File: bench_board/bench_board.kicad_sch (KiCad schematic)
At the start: 55 parts, among them J1 BATT_4S, J2 BOOT0_JUMPER, J3 USB-C, J4 CRSF_UART, J5 DSHOT_M1-M4, J6 SWD, J7 RX_PWR_5V, J8 TELEM_TX, J9 EXPANSION_BUS, U1 STM32F405RGT6, U2 TPS54336ADDA, U4 MPU-6000, U5 USBLC6-2SC6, U6 MT3608, Y1 8MHz

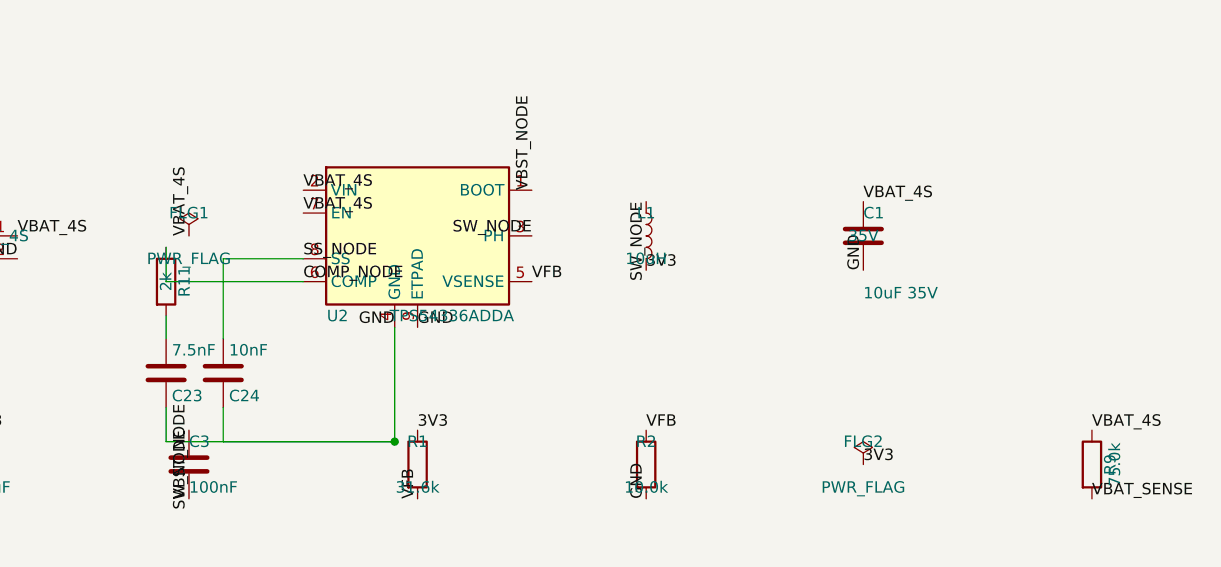
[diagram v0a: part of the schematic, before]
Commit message: Item 2: board blocker burn-down -- C23, Y1, C1, holes, net parity
BLOCKER 4 CLEARED -- C23's net existed nowhere. The buck's compensation
network is COMP_NODE -> R11 -> [nothing] -> C23 -> GND: the junction
between R11 pin 2 and C23 pin 1 had no wire, so the TPS54336's control
loop was not connected. Added the wire and a COMP_RC net label; ERC still
0/0, and the net now appears on the board (52 nets, was 51). C23 is gone
from the parity report.

Y1 -- the board carried a 4-pin 3225 crystal footprint under a 2-PIN
schematic symbol, which is why pads 3/4 were permanently unmatched in
every sync. The only Basic-library 8MHz part (C115962) is a 2-pin
SMD-5032. Delete-and-replaced to Crystal_SMD_5032-2Pin_5.0x3.2mm: fixes
the pad mismatch AND removes a JLCPCB Extended setup fee. Pad count
verified 2.

C1 -- respecified per the review's correction. The old note confused
voltage rating with DC-bias derating. Now 1210 / 50V / X7R (Murata
GRM32ER71H106KA12L) with the requirement written as CAPACITANCE AT
16.8V BIAS and an explicit instruction to read the vendor's C-vs-Vdc
curve before ordering. Footprint delete-and-replaced 0805 -> 1210.

MOUNTING HOLES -- fixing a defect I introduced last batch. The 30.5x30.5
pattern placed them ON TOP of nine components (D1, J2, R12, R13, C2, J4,
L1, R1, U2, C6, J6, R3): I validated one component's position virtually
and never re-ran the full overlap check after placing the holes. Moved
to (4.5,19), (75.5,16), (4.5,55.5), (75.5,41) -- found by scanning every
courtyard, verified 0 overlaps. Also moved Y1 and L1, which were
overlapping U1 and U2. Board is now 0 courtyard overlaps. MH silkscreen
text hidden (its bbox is 20mm wide for a 6mm hole and hung off the edge).

NET PARITY -- 262 -> 88 parity issues. All 199 net_conflicts were the
same uniform difference: the board stored bare net names, KiCad's
netlister uses the sheet-path form (GND vs /GND), across 52 nets with no
genuine mismatch hiding among them. Renamed every board net reference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
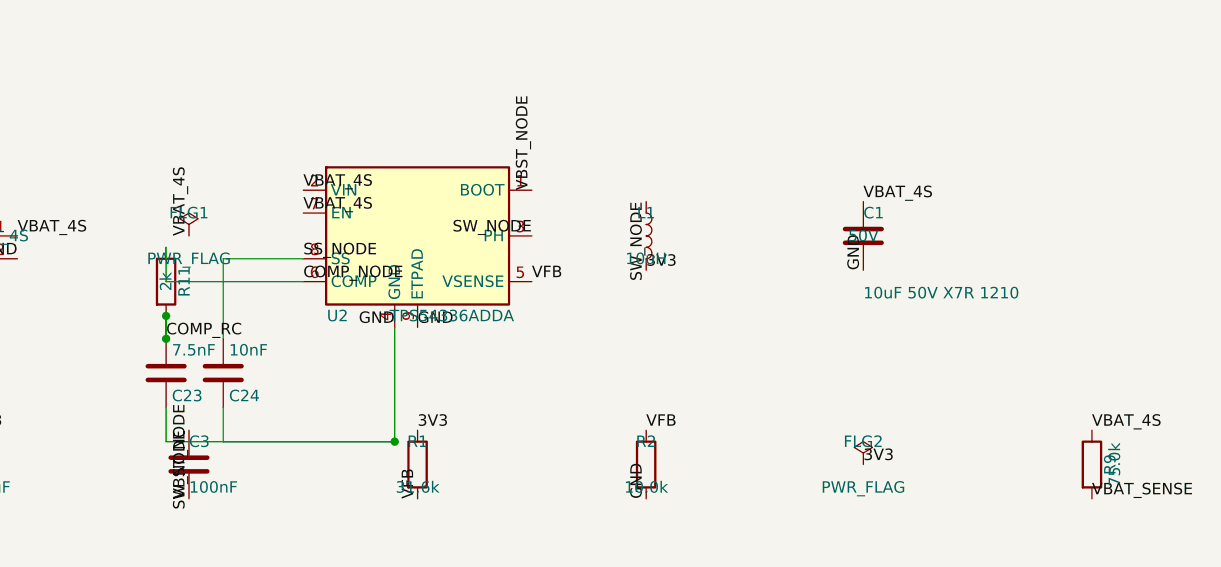
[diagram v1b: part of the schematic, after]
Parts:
- C1: value 10uF 35V -> 10uF 50V X7R 1210; footprint Capacitor_SMD:C_0805_2012Metric -> Capacitor_SMD:C_1210_3225Metric; Dielectric (none) -> X7R; MPN (none) -> GRM32ER71H106KA12L; Manufacturer (none) -> Murata; Notes (none) -> VBAT_4S input bulk, 16.8V max. SPEC IS CAPACITANCE AT BIAS,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; Voltage 35V -> 50V
- Y1: footprint Crystal:Crystal_SMD_3225-4Pin_3.2x2.5mm -> Crystal:Crystal_SMD_5032-2Pin_5.0x3.2mm; JLCPCB_PN (none) -> C115962; LCSC (none) -> C115962; Manufacturer (none) -> TXC; Notes (none) -> 8MHz +/-10ppm, SMD-5032-2P. Switched from a 3225-4Pin footp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
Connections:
- net COMP_RC: now reaches C23.1, R11.2
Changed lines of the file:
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@@
 			)
 		)
-		(property "Value" "10uF 35V"
+		(property "Value" "10uF 50V X7R 1210"
 			(at 449.58 55.88 0)
 			(show_name no)
@@
 			)
 		)
-		(property "Footprint" "Capacitor_SMD:C_0805_2012Metric"
+		(property "Footprint" "Capacitor_SMD:C_1210_3225Metric"
 			(at 450.545 45.72 0)
 			(hide yes)
@@
 			)
 		)
-		(property "Voltage" "35V"
+		(property "Voltage" "50V"
 			(at 449.58 49.53 0)
 			(effects
@@
 			)
 		)
+    (property "Dielectric" "X7R" (at 449.58 49.53 0)
+      (effects (font (size 1.27 1.27)) (hide yes))
+    )
+    (property "Manufacturer" "Murata" (at 449.58 49.53 0)
+      (effects (font (size 1.27 1.27)) (hide yes))
+    )
+    (property "MPN" "GRM32ER71H106KA12L" (at 449.58 49.53 0)
+      (effects (font (size 1.27 1.27)) (hide yes))
+    )
+    (property "Notes" "VBAT_4S input bulk, 16.8V max. SPEC IS CAPACITANCE AT BIAS, NOT NAMEPLATE: an MLCC's value collapses under DC bias regardless of its voltage rating, so '10uF' alone is meaningless here. Was 0805 25V, which at 16.8V retains only a small fraction. Moved to 1210/50V X7R on 2026-08-17 because bias derating is driven by case size and dielectric, not by the rating. MUST VERIFY the derated value on Murata SimSurfing (or the vendor's own C-vs-Vdc curve) before ordering and confirm it meets the TPS54336A input-capacitance requirement; do not accept a substitute chosen on nameplate value alone." (at 449.58 49.53 0)
+      (effects (font (size 1.27 1.27)) (hide yes))
+    )
 		(pin "1"
 		)
@@
 			)
 		)
-		(property "Footprint" "Crystal:Crystal_SMD_3225-4Pin_3.2x2.5mm"
+		(property "Footprint" "Crystal:Crystal_SMD_5032-2Pin_5.0x3.2mm"
 			(at 449.58 199.39 0)
 			(hide yes)
@@
 			)
 		)
+    (property "LCSC" "C115962" (at 449.58 199.39 0)
+      (effects (font (size 1.27 1.27)) (hide yes))
+    )
+    (property "JLCPCB_PN" "C115962" (at 449.58 199.39 0)
+      (effects (font (size 1.27 1.27)) (hide yes))
+    )
+    (property "Manufacturer" "TXC" (at 449.58 199.39 0)
+      (effects (font (size 1.27 1.27)) (hide yes))
+    )
+    (property "Notes" "8MHz +/-10ppm, SMD-5032-2P. Switched from a 3225-4Pin footprint 2026-08-17: the symbol is a 2-pin crystal, so the 4-pin footprint left pads 3/4 permanently unmatched, and the only Basic-library 8MHz part is this 2-pin 5032. Verify the part number against a live JLCPCB page before ordering -- it came from a community snapshot of the Basic library, not an authoritative source." (at 449.58 199.39 0)
+      (effects (font (size 1.27 1.27)) (hide yes))
+    )
 		(pin "1"
 		)
@@
 		(effects
 			(font
+				(size 1.27 1.27)
+			)
+			(justify left bottom)
+		)
+	)
+	(wire
+		(pts
+			(xy 372.11 58.42) (xy 372.11 60.959999999999994)
+		)
+		(stroke
+			(width 0)
+			(type default)
+		)
+	)
+	(junction
+		(at 372.11 58.42)
+		(diameter 0)
+		(color 0 0 0 0)
+	)
+	(junction
+		(at 372.11 60.96)
+		(diameter 0)
+		(color 0 0 0 0)
+	)
+	(label "COMP_RC"
+		(at 372.11 60.959999999999994 0)
+		(effects
+			(font

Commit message: Item 5 (hardware): buzzer on PA8 -- low-side MOSFET, placed and part-routed
Q1 AO3400A low-side switch, R14 100R gate series, R15 10k pull-down, D2
1N4148W flyback, C27 10uF local bulk, J10 2-pin header. PA8 chosen over
several other free GPIOs because it is TIM1_CH1 and TIM1 is unused, so a
passive buzzer with real tones stays possible with no board change. PA8's
stale no-connect flag removed; ERC is 0/0.

An F4 pin is rated 25 mA and a 12 mm buzzer draws 30-90 mA, so the FET is
not optional. D2 is fitted even though a piezo buzzer would not need it --
two cents to make the board buzzer-type-independent.

THE PLACEMENT WAS WRONG FIRST TIME. Q1 and C27 landed on top of a 15.7 mm
NRST track from J6 pin 4; DRC caught it as a /NRST <-> /BUZZER_SW short.
The region had been picked by reading the component list, and a component
list says nothing about routed copper -- check_placement_clearance does
not either, it classifies bodies and courtyards, not tracks.

scripts/padclear.py now measures every new pad against every segment and
via on the layers that pad occupies. It then caught two more that would
have shipped: a /BUZZER_SW diagonal passing 0.011 mm from J10's 5V pad,
and a GND via sited OUTSIDE the GND pour (the pour stops at y~58.0) --
the same class as this project's earlier fanout-via blocker, fixed the
same way, point-in-polygon against real filled_polygon geometry. The
checker itself had the KiCad rotation sign backwards on first use and was
verifying J10's pads at mirrored coordinates; corrected.

Routed and verified: BUZZER_GATE, BUZZER_SW, the local 5V chain, and GND
with two stitching vias both confirmed >=0.60 mm inside the GND pour.
NOT routed: BUZZER_GPIO (U1.41 -> R14.1, ~20 mm across the busy area) and
the 5V feed from J7. Until the first of those exists the buzzer cannot be
driven at all, which the doc says in those words.

kicad-cli DRC 46 -> 64, unconnected 13 -> 15. The +2 unconnected are
exactly the two nets above. +12 of the +18 violations are th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
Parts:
- added C27: 10uF 16V, Capacitor_SMD:C_0805_2012Metric, symbol Device:C
- added D2: 1N4148W, Diode_SMD:D_SOD-123, symbol Diode:1N4148W
- added J10: BUZZER, Connector_PinHeader_2.54mm:PinHeader_1x02_P2.54mm_Vertical, symbol Connector:Conn_01x02_Pin
- added Q1: AO3400A, Package_TO_SOT_SMD:SOT-23, symbol Transistor_FET:AO3400A
- added R14: 100R, Resistor_SMD:R_0402_1005Metric, symbol Device:R
- added R15: 10k, Resistor_SMD:R_0402_1005Metric, symbol Device:R
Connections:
- net 5V_RX: now also C27.1, D2.1 (K), J10.1 (Pin_1)
- net GND: now also C27.2, Q1.2 (S), R15.2
- net BUZZER_GPIO: now reaches U1.41 (PA8)
- net BUZZER_GPIO: now also R14.1
- new net BUZZER_GATE: Q1.1 (G), R14.2, R15.1
- new net BUZZER_SW: D2.2 (A), J10.2 (Pin_2), Q1.3 (D)
- no-connect marks 24 -> 23

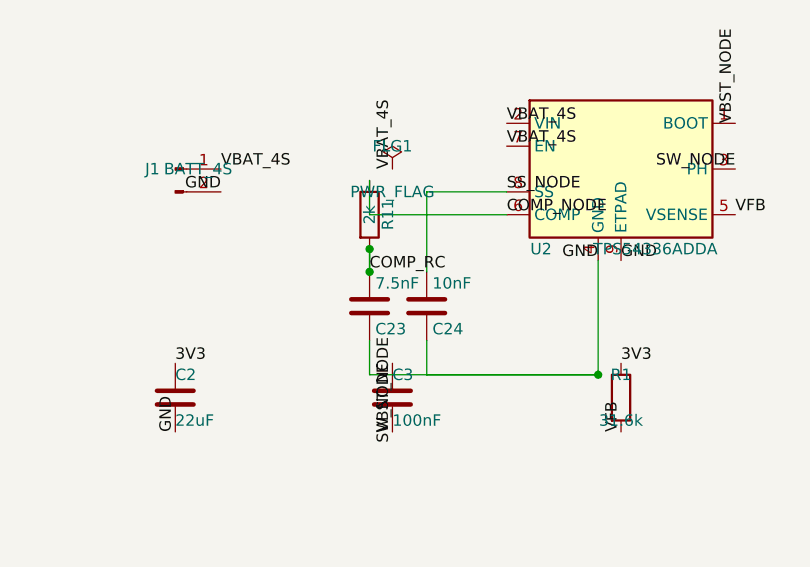
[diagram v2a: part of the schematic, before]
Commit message: C23: 7.5nF -> 8.2nF (LCSC C107032) per ngspice loop-gain study; ERC 0, guard 53/2/93
8.2nF raises phase margin at both corners (+1.2 deg at 14.8V and 25.2V)
where 6.8nF lowers it; crossover unchanged within 0.5%. JLCPCB stocks no
7.5nF MLCC. Study harness and results in sim/. Board+schematic value
edited together; guard re-run PASS 53/2/93, ERC 0 violations.

Co-Authored-By: Claude Fable 5 <noreply@anthropic.com>
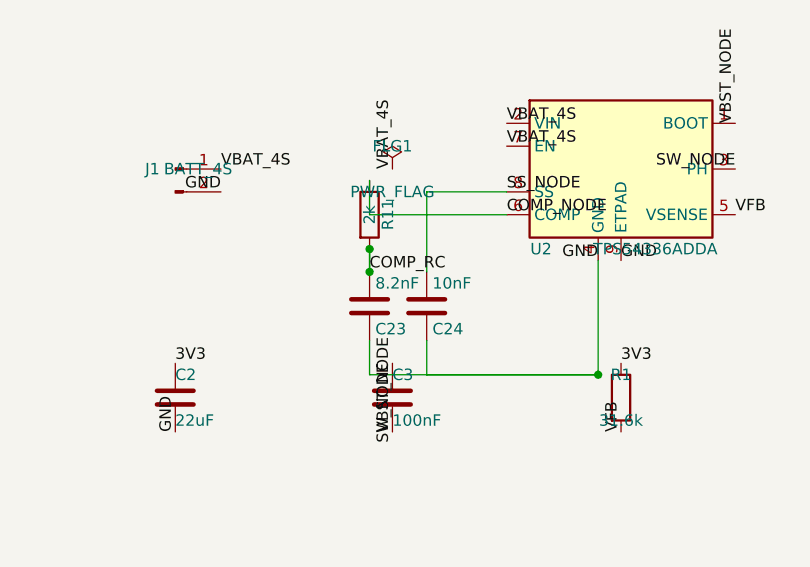
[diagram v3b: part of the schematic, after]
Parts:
- C23: value 7.5nF -> 8.2nF
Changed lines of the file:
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@@
 			)
 		)
-		(property "Value" "7.5nF"
+		(property "Value" "8.2nF"
 			(at 372.745 62.23 0)
 			(show_name no)

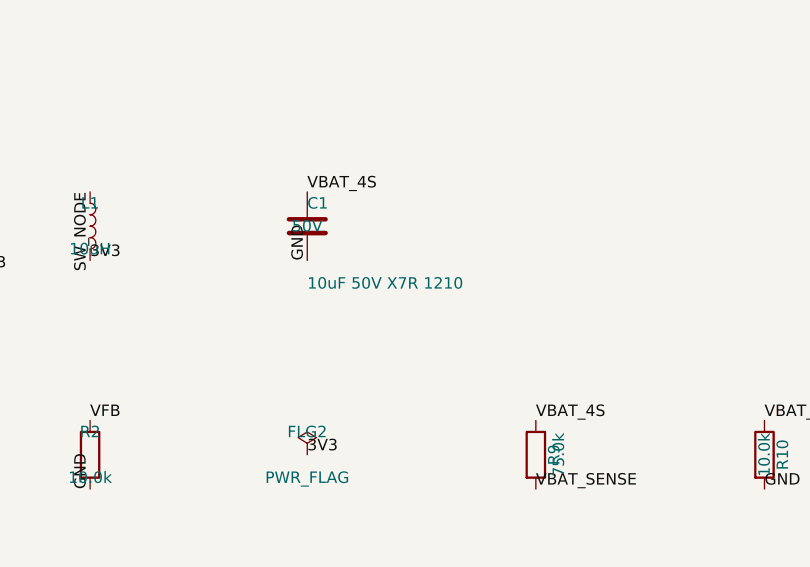
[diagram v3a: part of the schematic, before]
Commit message: Batch 6 review fixes: the bench fix that could not be performed, and seven more
Independent review (fresh agent, read-only) returned 1 BLOCKER, 3 HIGH,
6 MEDIUM, 6 LOW. Acted on here:

- BLOCKER: order sheet's 'sub-millimetre solder bridges' for the two
  remaining unconnected pads misread the DRC track-LENGTH field as a
  gap. Re-measured from the board file: U4.1->U4.18 is 3.9mm, U1.48->
  C20.2 is 7.4mm. Remediation rewritten as wire jumpers with routes,
  wire spec, and honest time budget; misread acknowledged in place.
- HIGH: C24.1 removed from the mandatory via-in-pad remark (reviewer
  re-derivation with exact roundrect geometry: nearest via clears by
  0.153mm; false positive). C2.1 near-tangent (0.014mm) added instead.
- HIGH: check_cpl.py default FABDIR and the falsifiability cpl case
  pointed at 17c (were validating the superseded 17b); both re-run,
  PASS/exit 0.
- HIGH: README gate numbers corrected (assembly rows without LCSC
  8->0, not 9->3).
- MEDIUM: board via-protection metadata set (capping yes)(filling yes)
  to match the mandatory fab spec; guard PASS 53/2/93 unchanged.
- MEDIUM: SPICE harness header's wrong PM formula (180-|phase|)
  replaced with the corrected convention note; the study script was
  already right.
- MEDIUM: the 'no 7.5nF at JLCPCB' premise was FALSE as stated -- two
  C0G parts exist in 0603/0805, none in 0402. Corrected in the study
  output, script, and BOM; committed evidence in
  sim/c23_jlcpcb_7p5nF_search.txt; empty _mlcc_head.csv removed. The
  8.2nF choice stands on measured margin + avoided footprint edit.
- MEDIUM: L1/L2 and Y1 verify-before-paying checks surfaced in the
  order sheet's matching step.
- Counts/typos: 51 placed parts, 11 Extended numbers (3), copper-
  edge 0.269/0.298mm, C1 CPL value X7S (board+sch edited, ERC 0,
  guard PASS, CPL/BOM/DRC regenerated, check_cpl PASS).

Not changed, documented as accepted: min_through_hole_diameter 0.15
now also floors component PTH holes (finding 9); guard remains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
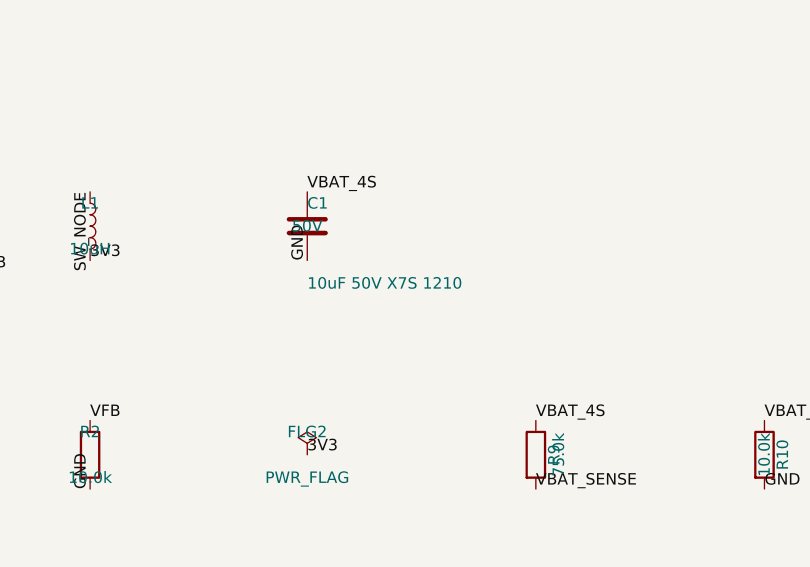
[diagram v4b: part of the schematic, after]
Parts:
- C1: value 10uF 50V X7R 1210 -> 10uF 50V X7S 1210
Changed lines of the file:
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@@
 			)
 		)
-		(property "Value" "10uF 50V X7R 1210"
+		(property "Value" "10uF 50V X7S 1210"
 			(at 449.58 55.88 0)
 			(show_name no)
